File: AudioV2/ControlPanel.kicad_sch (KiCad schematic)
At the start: 36 parts, among them SW1 PWR SW, U1 Pico 2 / RP2350, U2 PT2314, U3 PGA2310PA HP, U4 PGA2310PA LINE, U5 BP5293-50 +5V, U6 OLED ctrl I2C

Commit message: AudioV2: embed lib_symbols on all child schematics (KiCad 10)
ControlPanel, RelayBoard, and OutputStage had empty lib_symbols and
legacy symbol_inst without pin UUIDs — same pads-only issue as PowerModule.

- Extend sch_helpers: SYMBOL_SOURCES aliases, auto pin_numbers_for,
  BP5293 from Audio/, sanitize (type solid), sub-symbol rename on alias
- Regenerate all sheets via wire_circuit_design.py (power/control/relay/output)
- Fix Pico lib_id to MCU_Module:RaspberryPi_Pico (KiCad 10 name)
- SSD1306-128x64 embeds ER_OLEDM0.91 graphic under alias name
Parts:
- removed U1: Pico 2 / RP2350, symbol MCU_Module:Raspberry_Pi_Pico
- added U1: Pico 2 / RP2350, symbol MCU_Module:RaspberryPi_Pico
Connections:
- new net: R202.1, R203.2
- new net: C207.1, C208.2
- new net: C211.1, R205.1
- new net: C211.2, R204.1, R205.2
- new net: U3.10 (AGNDR), U4.2 (~{CS})
- new net: U3.2 (~{CS}), U4.16 (V_{IN}L)
- new net: U3.6 (SCLK), U4.15 (AGNDL)
- new net: U3.7 (SDO), U4.8 (~{MUTE})
- new net: U3.9 (V_{IN}R), U4.6 (SCLK)
- new net: C205.1, C206.2
- new net: U1.13 (GND), U1.18 (GND), U1.23 (GND), U1.28 (GND), U1.3 (GND), U1.38 (GND), U1.8 (GND)

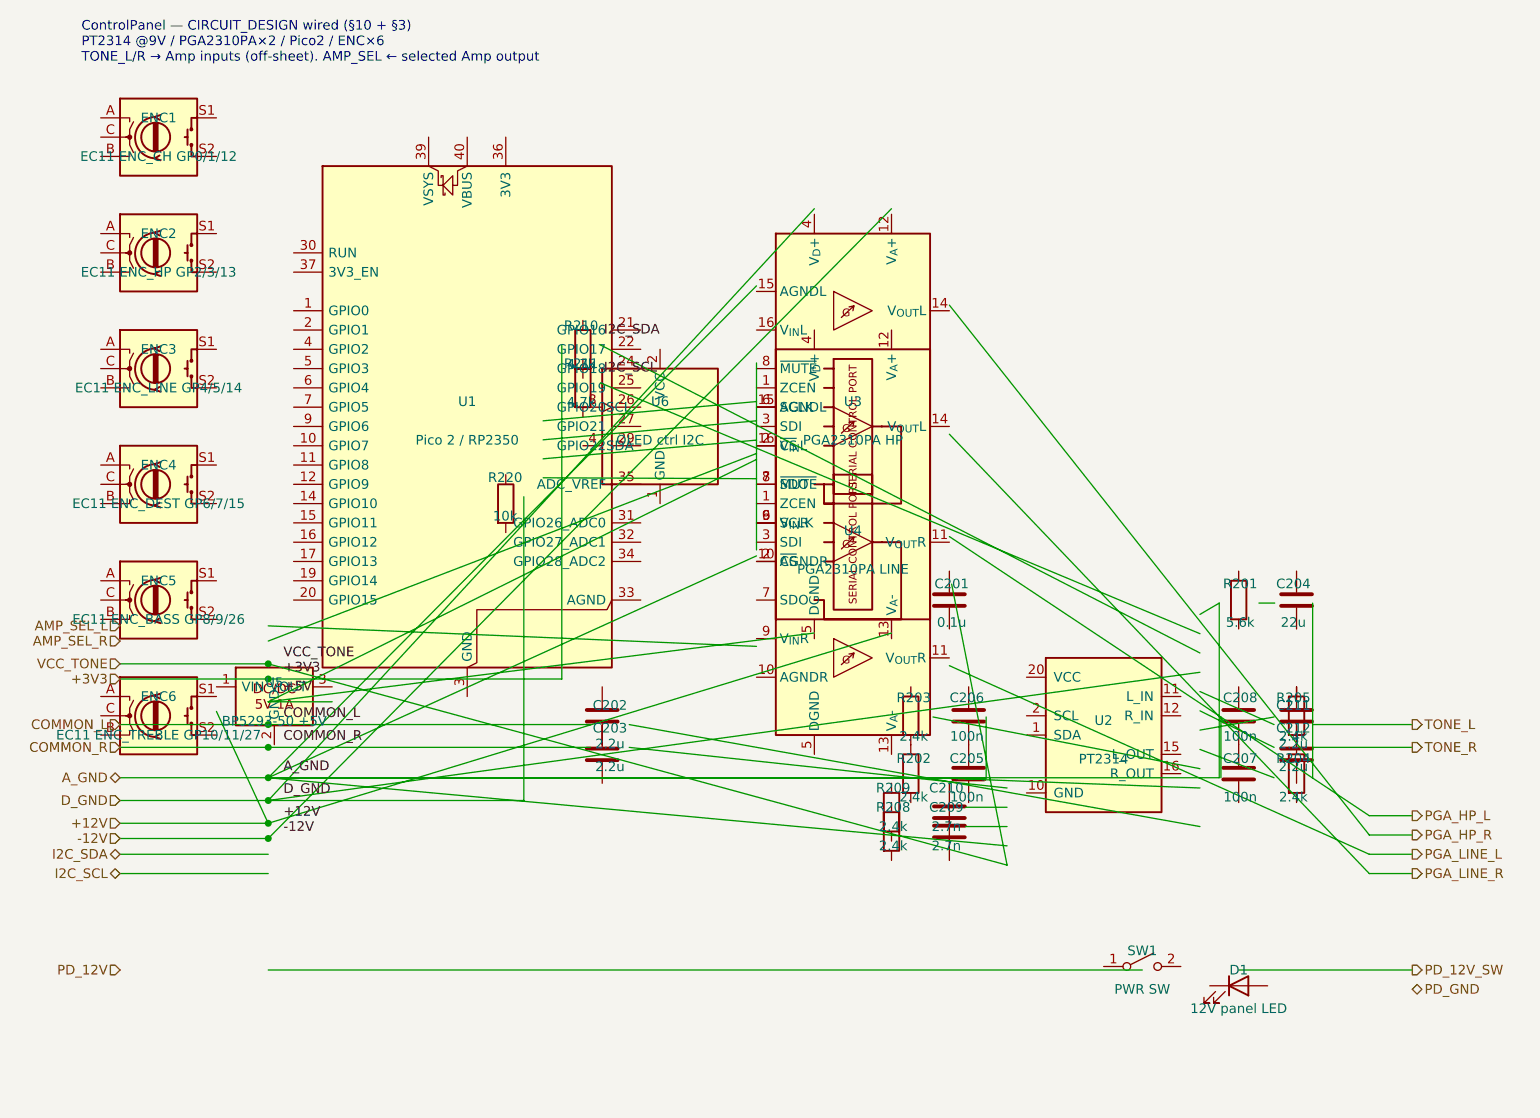
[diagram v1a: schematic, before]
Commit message: feat(AudioV2): 手回し音量構成へ回路図を改訂
- PT2314 を Princeton DS どおり 28pin DIP シンボルに再作成
- PGA2310 / DEST ラッチング / ENC×6 を削除
- OutputStage: SW_DP3T + A50k Dual×2（AMP_SEL→PHONE/LINE）
- ControlPanel: ENC×3 + DEST ラダー(10k/10k/1k) + LED
- CIRCUIT_DESIGN.md を DS 照合・手回し方針に更新
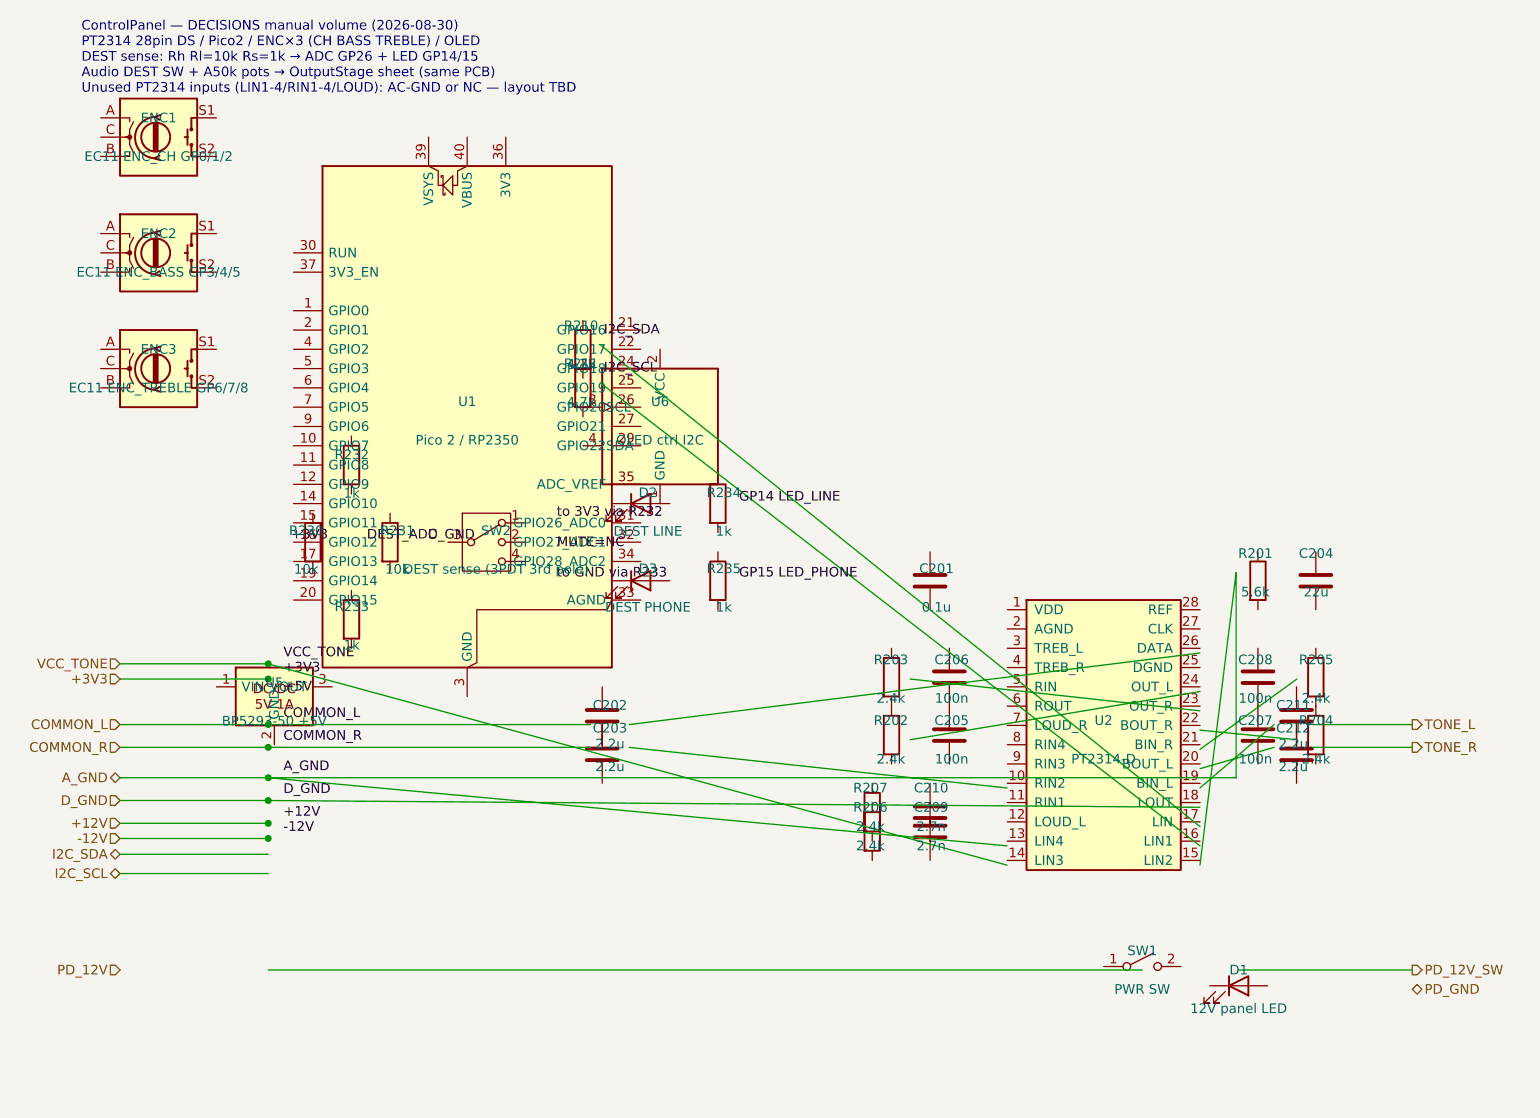
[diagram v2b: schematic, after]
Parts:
- removed ENC4: EC11 ENC_DEST GP6/7/15, symbol Device:RotaryEncoder_Switch
- removed ENC5: EC11 ENC_BASS GP8/9/26, symbol Device:RotaryEncoder_Switch
- removed ENC6: EC11 ENC_TREBLE GP10/11/27, symbol Device:RotaryEncoder_Switch
- removed R208, R209: 2.4k, symbol Device:R
- removed R220: 10k, symbol Device:R
- removed U3: PGA2310PA HP, symbol Audio:PGA2310PA
- removed U4: PGA2310PA LINE, symbol Audio:PGA2310PA
- added D2: DEST LINE, symbol Device:LED
- added D3: DEST PHONE, symbol Device:LED
- added R206, R207: 2.4k, symbol Device:R
- added R230, R231: 10k, symbol Device:R
- added R232, R233, R234, R235: 1k, symbol Device:R
- added SW2: DEST sense (3PDT 3rd pole), symbol Switch:SW_SP3T
- ENC1: value EC11 ENC_CH GP0/1/12 -> EC11 ENC_CH GP0/1/2
- ENC2: value EC11 ENC_HP GP2/3/13 -> EC11 ENC_BASS GP3/4/5
- ENC3: value EC11 ENC_LINE GP4/5/14 -> EC11 ENC_TREBLE GP6/7/8
- U2: value PT2314 -> PT2314-D
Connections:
- net at C211.1: no longer R205.1
- net at R204.1, R205.2: no longer C211.2
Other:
- note added: "ControlPanel — DECISIONS manual volume (2026-08-30) PT2314 28pin DS / Pico2 / ENC×3 (CH BASS TREBLE) / OLED DEST sense: Rh Rl=10k Rs=1k → ADC GP26 + LED GP14/15 Audio DEST SW + A50k pots → OutputStage sheet (same PCB) Unused PT2314 inputs (LIN1-4/RIN1-4/LOUD): AC-GND or NC — layout TBD"
- note removed: "ControlPanel — CIRCUIT_DESIGN wired (§10 + §3) PT2314 @9V / PGA2310PA×2 / Pico2 / ENC×6 TONE_L/R → Amp inputs (off-sheet). AMP_SEL ← selected Amp output"

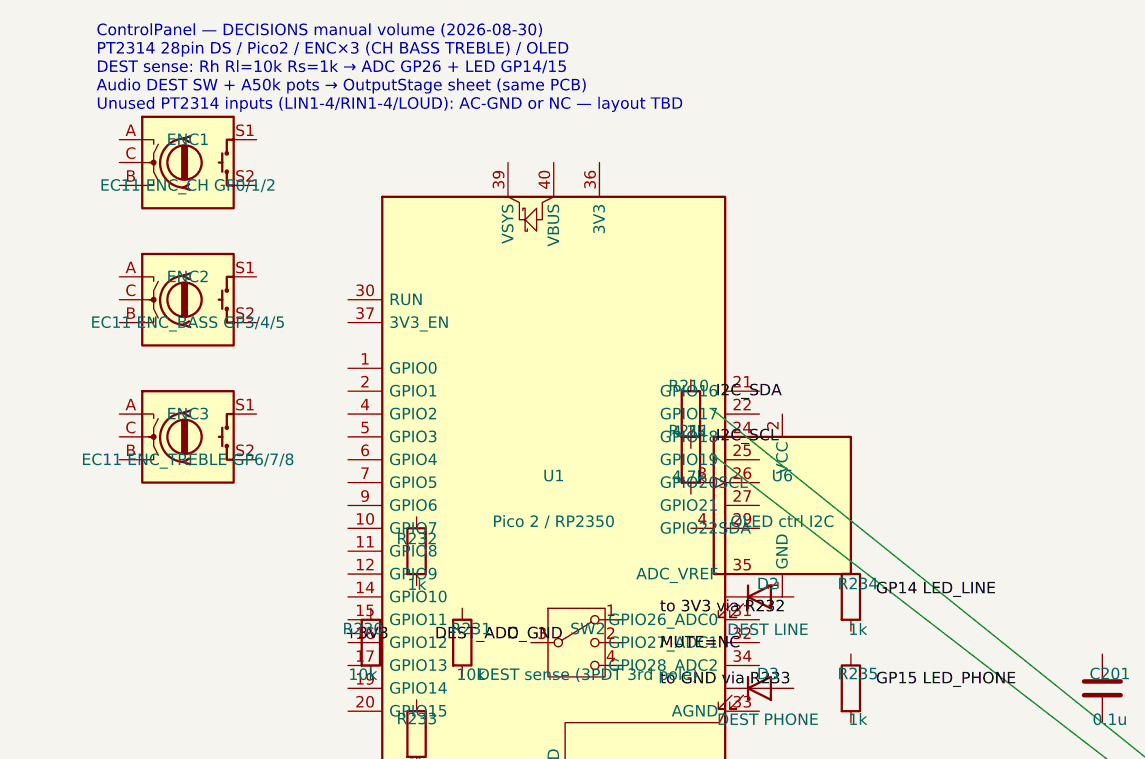
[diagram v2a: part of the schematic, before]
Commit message: fix(AudioV2): WP-B embed flatten / OLED / PowerModule 一次二次分離
WP-A A1/A2 も取り込み: AudioV2.kicad_sym の二重 embedded_fonts 除去と
PT2314 float 座標正規化。embed_lib_symbols は extends を親ピン付き定義へ
flatten。OLED は Conn_01x04 ヘッダに置換。PowerModule は PD_GND と
PD_12V_SW/F1 の Y 衝突を解消し、7809 GND→A_GND、R.C. オープン。

Co-authored-by: m_arino <indare@users.noreply.github.com>
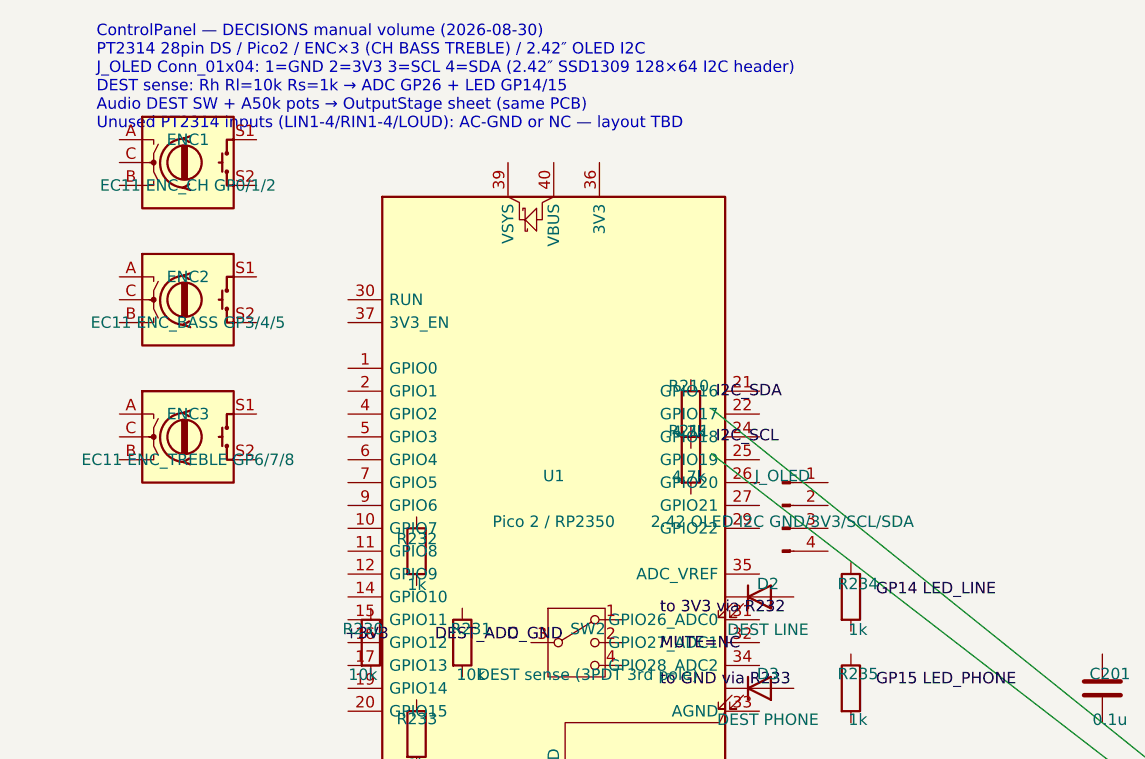
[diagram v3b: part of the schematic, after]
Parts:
- removed U6: OLED ctrl I2C, symbol Display_Graphic:SSD1306-128x64
- added J_OLED: 2.42 OLED I2C GND/3V3/SCL/SDA, symbol Connector:Conn_01x04_Pin
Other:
- note added: "ControlPanel — DECISIONS manual volume (2026-08-30) PT2314 28pin DS / Pico2 / ENC×3 (CH BASS TREBLE) / 2.42″ OLED I2C J_OLED Conn_01x04: 1=GND 2=3V3 3=SCL 4=SDA (2.42″ SSD1309 128×64 I2C header) DEST sense: Rh Rl=10k Rs=1k → ADC GP26 + LED GP14/15 Audio DEST SW + A50k pots → OutputStage sheet (same PCB) Unused PT2314 inputs (LIN1-4/RIN1-4/LOUD): AC-GND or NC — layout TBD"
- note removed: "ControlPanel — DECISIONS manual volume (2026-08-30) PT2314 28pin DS / Pico2 / ENC×3 (CH BASS TREBLE) / OLED DEST sense: Rh Rl=10k Rs=1k → ADC GP26 + LED GP14/15 Audio DEST SW + A50k pots → OutputStage sheet (same PCB) Unused PT2314 inputs (LIN1-4/RIN1-4/LOUD): AC-GND or NC — layout TBD"
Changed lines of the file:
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@@
 	(generator_version "10.0")
 	(paper "A4")
-	(text "ControlPanel — DECISIONS manual volume (2026-08-30)\nPT2314 28pin DS / Pico2 / ENC×3 (CH BASS TREBLE) / OLED\nDEST sense: Rh Rl=10k Rs=1k → ADC GP26 + LED GP14/15\nAudio DEST SW + A50k pots → OutputStage sheet (same PCB)\nUnused PT2314 inputs (LIN1-4/RIN1-4/LOUD): AC-GND or NC — layout TBD"
+	(text "ControlPanel — DECISIONS manual volume (2026-08-30)\nPT2314 28pin DS / Pico2 / ENC×3 (CH BASS TREBLE) / 2.42″ OLED I2C\nJ_OLED Conn_01x04: 1=GND 2=3V3 3=SCL 4=SDA (2.42″ SSD1309 128×64 I2C header)\nDEST sense: Rh Rl=10k Rs=1k → ADC GP26 + LED GP14/15\nAudio DEST SW + A50k pots → OutputStage sheet (same PCB)\nUnused PT2314 inputs (LIN1-4/RIN1-4/LOUD): AC-GND or NC — layout TBD"
 		(at 25.4 25.4 0)
 		(effects
@@
 	)
 	(symbol
-		(lib_id "Display_Graphic:SSD1306-128x64")
+		(lib_id "Connector:Conn_01x04_Pin")
 		(at 101.6 78.74 0)
 		(unit 1)
@@
 		(dnp no)
 		(fields_autoplaced yes)
-		(property "Reference" "U6"
+		(property "Reference" "J_OLED"
 			(at 101.6 75.46 0)
 			(show_name no)
@@
 			)
 		)
-		(property "Value" "OLED ctrl I2C"
+		(property "Value" "2.42 OLED I2C GND/3V3/SCL/SDA"
 			(at 101.6 80.54 0)
 			(show_name no)
@@
 			(project "AudioV2Case"
 				(path "/a1000001-0001-4001-8001-000000000001/a1000006-0006-4006-8006-000000000006"
-					(reference "U6")
+					(reference "J_OLED")
 					(unit 1)
 				)
